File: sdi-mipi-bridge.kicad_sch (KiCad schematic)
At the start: 215 parts, among them J1 112740-13, J2 112740-13, J3 WE_68715014522_ONE-SIDE, J4 GRPB052VWVN-RC, J5 GRPB041VWVN-RC, J6 GRPB052VWVN-RC, SW1 SW_DIP_x06, SW2 SW_DIP_x06, U1 MAX8902B, U2 GS2971A, U3 GS2988, U4 CrossLink_LIF-MD6000-6JMG80I, U5 SC18IS602BIPW, Y1 ABM7_27.000MH_D2Y_T

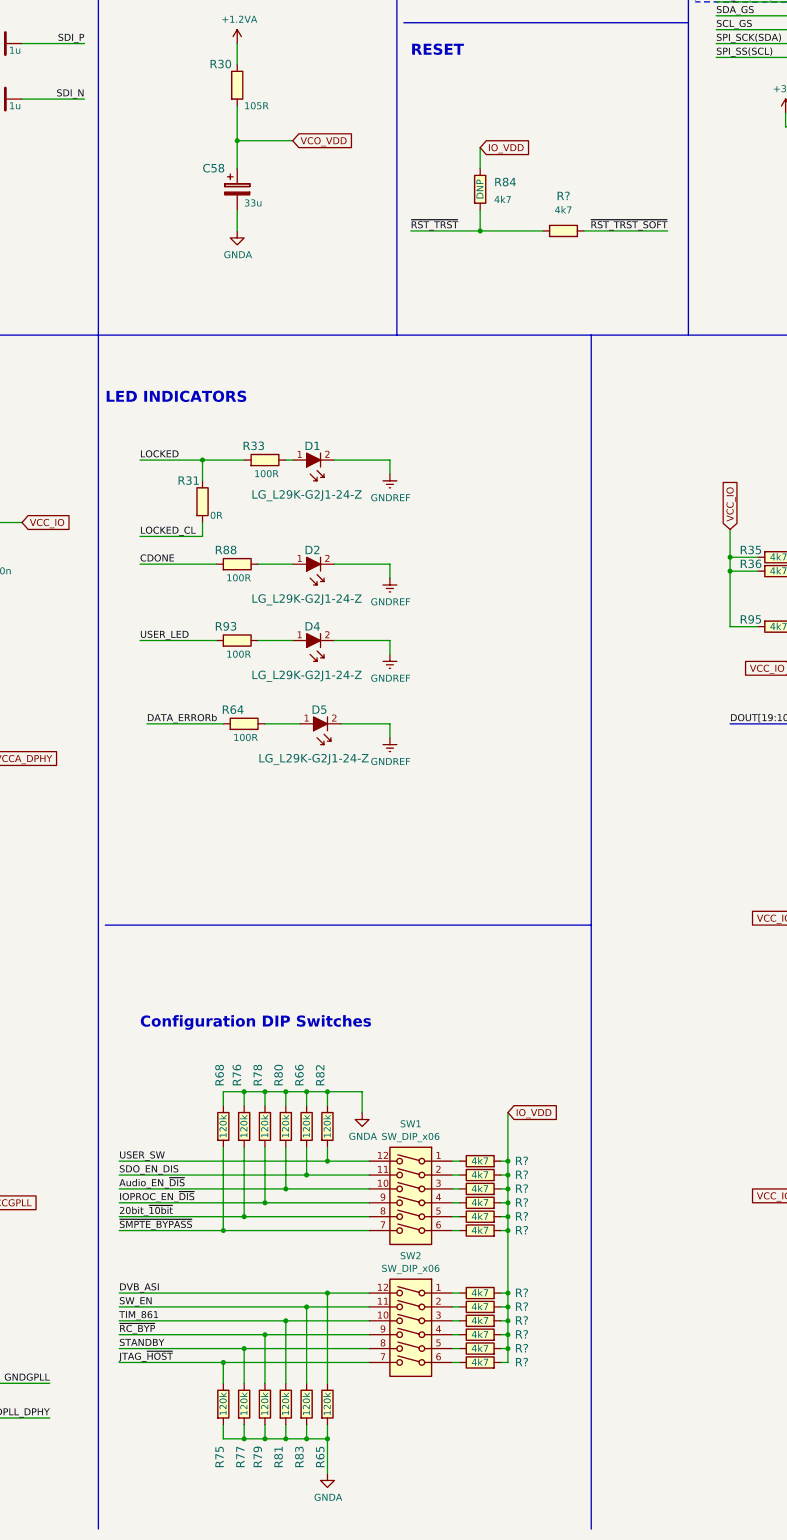
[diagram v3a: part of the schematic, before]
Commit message: Removed DIP switches and improved RST_TRST circuitry
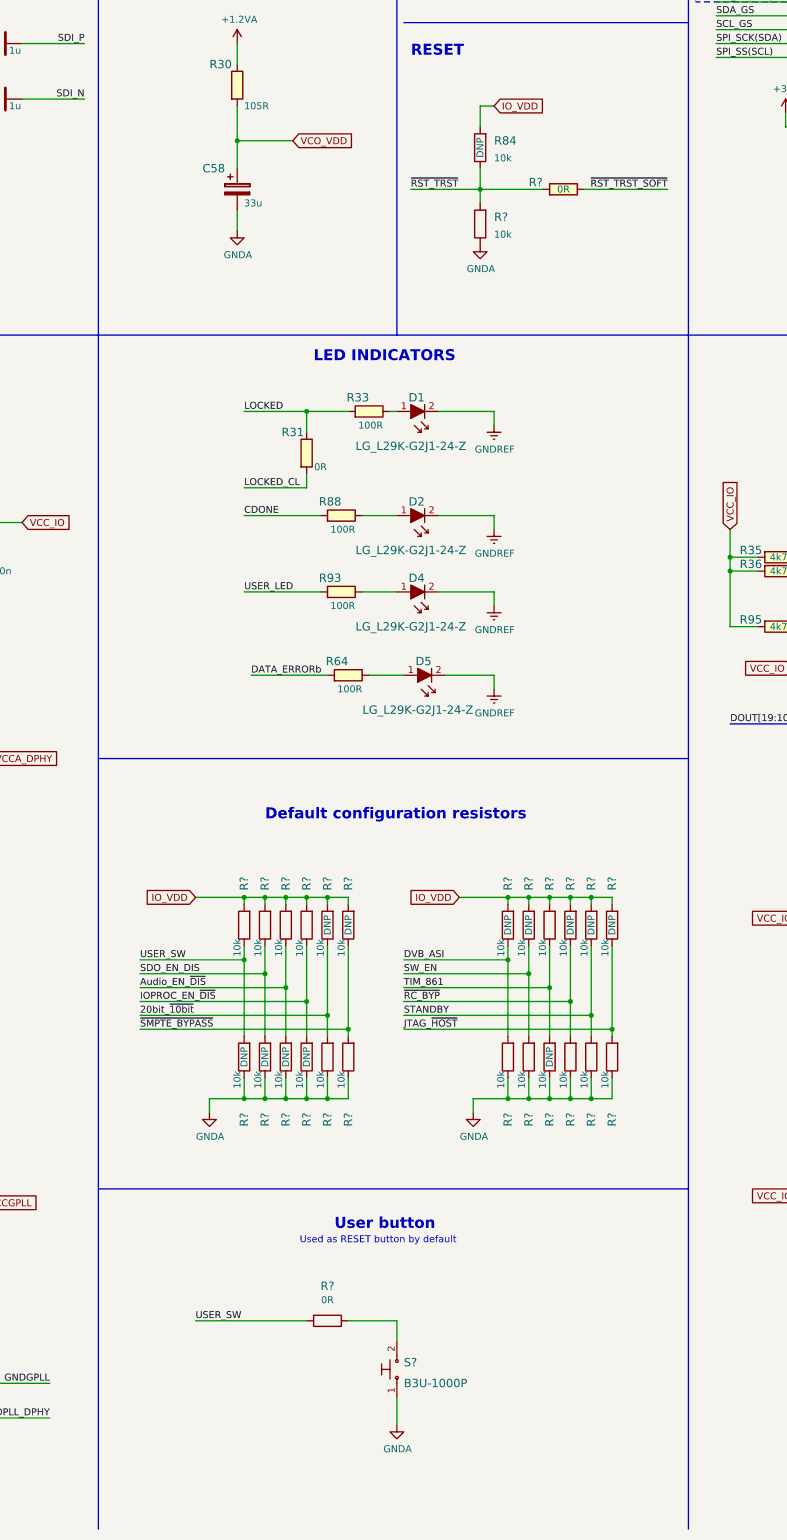
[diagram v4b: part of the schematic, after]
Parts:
- removed R65, R66, R68, R75, R76, R77, R78, R79, R80, R81, R82, R83: R_120k_0402, sdi-mipi-bridge-footprints:0402-res, symbol sdi-mipi-bridge:R_120k_0402
- removed R84, R? (x13): R_4k7_0402, sdi-mipi-bridge-footprints:0402-res, symbol sdi-mipi-bridge:R_4k7_0402
- removed SW1, SW2: SW_DIP_x06, sdi-mipi-bridge-footprints:SW_SPST_6_Slide_MCDHN-06F-T-V_P1.27mm, symbol sdi-mipi-bridge:SW_DIP_x06
- added R84, R? (x25): R_10k_0402, sdi-mipi-bridge-footprints:0402-res, symbol sdi-mipi-bridge:R_10k_0402
- added R?: R_0R_0402, sdi-mipi-bridge-footprints:0402-res, symbol sdi-mipi-bridge:R_0R_0402
- added R?: R_0R_0402, antmicro-footprints:0402-res, symbol antmicroResistors0402:R_0R_0402
- added S?: B3U-1000P, sdi-mipi-bridge-footprints:Switch_Tactile_SMD_B3U-1000P, symbol sdi-mipi-bridge:B3U-1000P
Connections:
- net 20bit_~{10bit}: now also R?.1, R?.2
- net Audio_EN_~{DIS}: now also R?.1, R?.2
- net DVB_ASI: now also R?.1, R?.2
- net GNDA: now also R?.1, R?.1, R?.1, R?.1, R?.1, R?.1, R?.1, R?.1, R?.1, R?.1, R?.1, R?.1, R?.1, S?.1
- net IOPROC_EN_~{DIS}: now also R?.1, R?.2
- net IO_VDD: now also R84.2, R?.2, R?.2, R?.2, R?.2, R?.2, R?.2, R?.2, R?.2, R?.2, R?.2, R?.2, R?.2
- net JTAG_~{HOST}: now also R?.1, R?.2
- net SDO_EN_DIS: now also R?.1, R?.2
- net STANDBY: now also R?.1, R?.2
- net SW_EN: now also R?.1, R?.2
- net TIM_861: now also R?.1, R?.2
- net USER_SW: now also R?.1, R?.1, R?.2
- net ~{RC_BYP}: now also R?.1, R?.2
- net ~{RST_TRST_SOFT}: now also R?.1
- net ~{RST_TRST}: now also R84.1, R?.2, R?.2
- net ~{SMPTE_BYPASS}: now also R?.1, R?.2
- new net: R?.2, S?.2
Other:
- note added: "Default configuration resistors"
- note added: "Used as RESET button by default"
- note added: "User button"
- note removed: "Configuration DIP Switches"
- moved on the sheet: D1, D2, D4, D5, R31, R33, R64, R88, R93

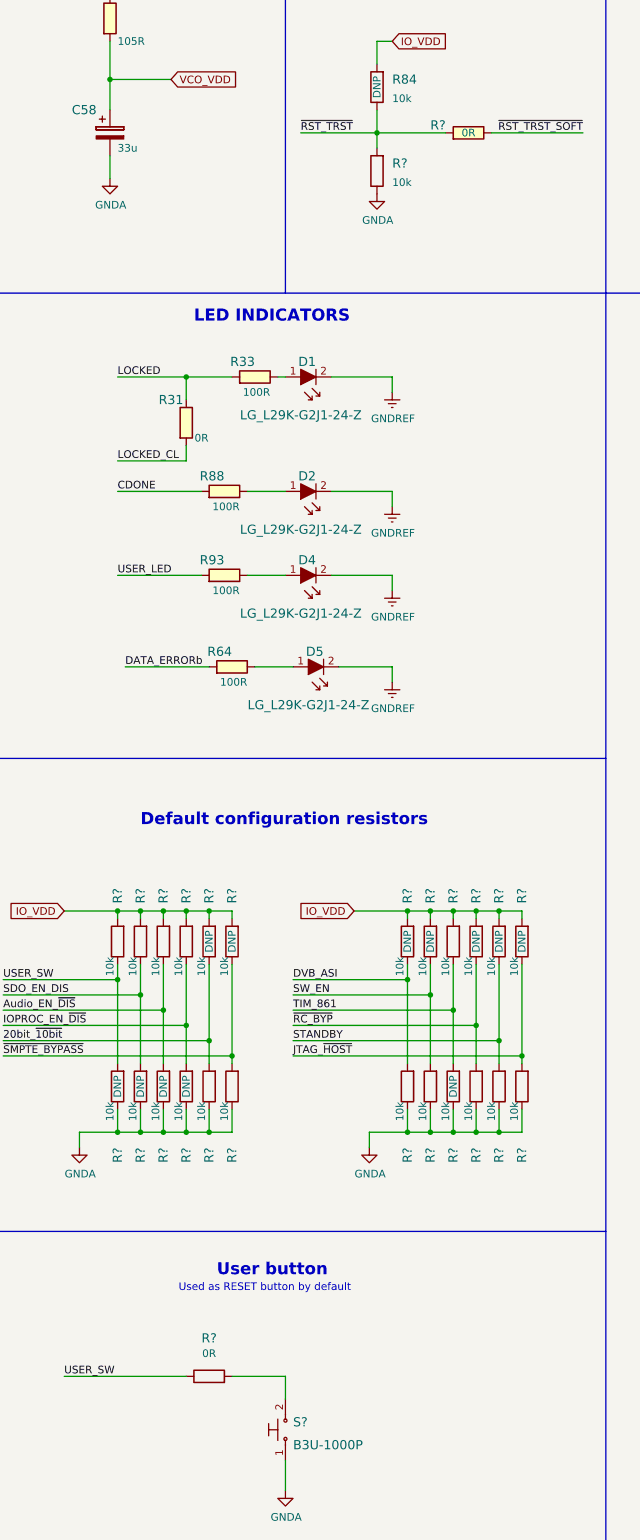
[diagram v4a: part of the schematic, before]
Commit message: Ported DIP switch and reset changes to the PCB
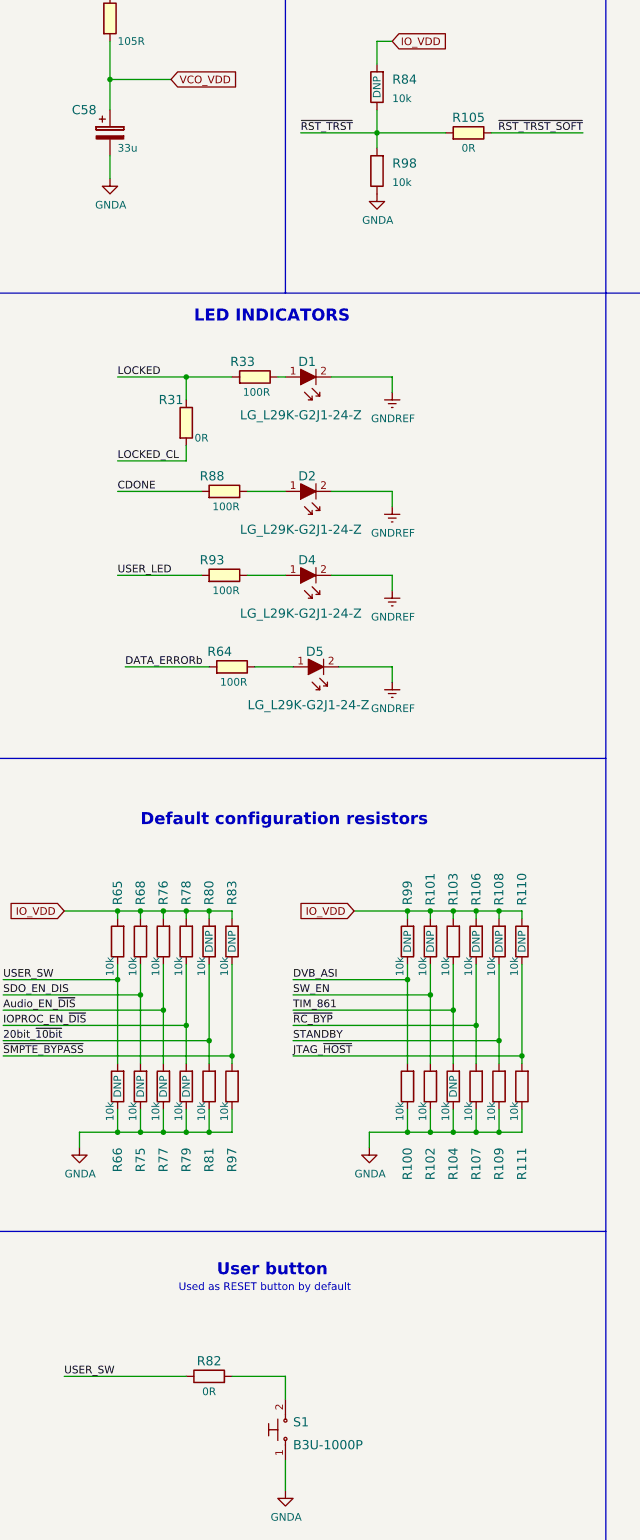
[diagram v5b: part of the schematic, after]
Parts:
- gave numbers to parts that had none: 28

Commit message: Unified configuration naming and changed DATA_ERROR name polarity
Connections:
- net DATA_ERRORb renamed ~{DATA_ERROR}
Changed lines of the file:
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@@
     (stroke (width 0) (type default) (color 0 0 0 0))
   )
-  (wire (pts (xy 327.66 251.46) (xy 341.63 251.46))
+  (wire (pts (xy 326.39 251.46) (xy 341.63 251.46))
     (stroke (width 0) (type default) (color 0 0 0 0))
   )
@@
     (effects (font (size 1.27 1.27)) (justify left bottom))
   )
+  (label "~{DATA_ERROR}" (at 431.8 311.15 0)
+    (effects (font (size 1.27 1.27)) (justify left bottom))
+  )
   (label "SDO_P" (at 31.75 90.17 0)
     (effects (font (size 1.27 1.27)) (justify left bottom))
@@
     (effects (font (size 1.27 1.27)) (justify right bottom))
   )
-  (label "DATA_ERRORb" (at 327.66 251.46 0)
-    (effects (font (size 1.27 1.27)) (justify left bottom))
-  )
   (label "SDOUT_TDO" (at 223.52 86.36 180)
     (effects (font (size 1.27 1.27)) (justify right bottom))
@@
     (effects (font (size 1.27 1.27)) (justify right bottom))
   )
+  (label "~{DATA_ERROR}" (at 326.39 251.46 0)
+    (effects (font (size 1.27 1.27)) (justify left bottom))
+  )
   (label "DPHY0_D3_P" (at 538.48 267.97 180)
     (effects (font (size 1.27 1.27)) (justify right bottom))
@@
     (effects (font (size 1.27 1.27)) (justify left bottom))
   )
-  (label "DATA_ERRORb" (at 31.75 60.96 0)
+  (label "~{DATA_ERROR}" (at 31.75 60.96 0)
     (effects (font (size 1.27 1.27)) (justify left bottom))
   )
@@
     (effects (font (size 1.27 1.27)) (justify left bottom))
   )
-  (label "DATA_ERRORb" (at 431.8 311.15 0)
-    (effects (font (size 1.27 1.27)) (justify left bottom))
-  )

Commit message: Remove 0R resistors from the fast signal lanes
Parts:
- removed R10, R11, R12, R13, R14, R15, R16, R44, R45, R46, R47, R48, R49, R50, R51, R52, R53, R54, R55, R56, R57, R58, R59, R60, R61, R62, R63, R7, R8, R9: R_0R_0402, sdi-mipi-bridge-footprints:0402-res, symbol sdi-mipi-bridge:R_0R_0402
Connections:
- net DOUT10 is gone; now on net D10: U4.J6 (PB29D/PCLKC1_1)
- net DOUT11 is gone; now on net D11: U4.J5 (PB34D/MIPI_CLKC1_0)
- net DOUT12 is gone; now on net D12: U4.J4 (PB38D)
- net DOUT13 is gone; now on net D13: U4.J3 (PB43D)
- net DOUT14 is gone; now on net D14: U4.E1 (PB34A/GR_PCLK1_0)
- net DOUT15 is gone; now on net D15: U4.K7 (PB29B/PCLKC1_0)
- net DOUT16 is gone; now on net D16: U4.K6 (PB29C/PCLKT1_1)
- net DOUT17 is gone; now on net D17: U4.K5 (PB34C/MIPI_CLKT1_0)
- net DOUT18 is gone; now on net D18: U4.K4 (PB38C)
- net DOUT19 is gone; now on net D19: U4.K3 (PB43C)
- net MIPI0_CLK_N is gone; now on net DPHY0_CLK_N: J3.10 (Pin_10)
- net MIPI0_CLK_P is gone; now on net DPHY0_CLK_P: J3.11 (Pin_11)
- net MIPI0_D0_N is gone; now on net DPHY0_D0_N: J3.7 (Pin_7)
- net MIPI0_D0_P is gone; now on net DPHY0_D0_P: J3.8 (Pin_8)
- net MIPI0_D1_N is gone; now on net DPHY0_D1_N: J3.5 (Pin_5)
- net MIPI0_D1_P is gone; now on net DPHY0_D1_P: J3.6 (Pin_6)
- net MIPI0_D2_N is gone; now on net DPHY0_D2_N: J3.3 (Pin_3)
- net MIPI0_D2_P is gone; now on net DPHY0_D2_P: J3.4 (Pin_4)
- net MIPI0_D3_N is gone; now on net DPHY0_D3_N: J3.1 (Pin_1)
- net MIPI0_D3_P is gone; now on net DPHY0_D3_P: J3.2 (Pin_2)
- net MIPI1_CLK_N is gone; now on net DPHY1_CLK_N: J3.28 (Pin_28)
- net MIPI1_CLK_P is gone; now on net DPHY1_CLK_P: J3.29 (Pin_29)
- net MIPI1_D0_N is gone; now on net DPHY1_D0_N: J3.25 (Pin_25)
- net MIPI1_D0_P is gone; now on net DPHY1_D0_P: J3.26 (Pin_26)
- net MIPI1_D1_N is gone; now on net DPHY1_D1_N: J3.23 (Pin_23)
- net MIPI1_D1_P is gone; now on net DPHY1_D1_P: J3.24 (Pin_24)
- net MIPI1_D2_N is gone; now on net DPHY1_D2_N: J3.21 (Pin_21)
- net MIPI1_D2_P is gone; now on net DPHY1_D2_P: J3.22 (Pin_22)
- net MIPI1_D3_N is gone; now on net DPHY1_D3_N: J3.19 (Pin_19)
- net MIPI1_D3_P is gone; now on net DPHY1_D3_P: J3.20 (Pin_20)
